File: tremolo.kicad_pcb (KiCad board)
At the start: 2 copper layers, 54 x 60 mm, 59 parts, among them J1 Jack-DC, J4 Conn_01x01_Female, J5 Conn_01x01_Female, Q1 MMBT3904, SW1 SW_Push, SW3 SW_Rotary8, SW4 SW_Rotary8, U1 TAPLFO3, U2 L78L05_SOT89, U3 VTL5C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

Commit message: cleanup
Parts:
- moved C11 32.7 mm to (92.6, 102.0), turned to 180 degrees
- moved SW1 24.1 mm to (92.5, 123.4), turned to 90 degrees
- moved R11 13.8 mm to (74.5, 102.2), turned to 0 degrees
- moved C8 12.8 mm to (113.5, 105.0)
- moved J1 12.1 mm to (72.3, 118.6), turned to 90 degrees
- moved R17 11.7 mm to (116.0, 105.0)
- moved C7 11.5 mm to (77.0, 105.2)
- moved J4 11.0 mm to (88.5, 138.5)
- moved R15 10.9 mm to (72.0, 105.2), turned to 90 degrees
- moved C6 10.7 mm to (80.6, 117.8)
- moved U2 9.86 mm to (79.8, 122.2)
- moved R31 8.94 mm to (108.0, 105.0), turned to -90 degrees
- moved C5 8.76 mm to (79.2, 127.2)
- moved R4 7.22 mm to (74.5, 111.2), turned to 90 degrees
- moved R18 6.27 mm to (113.0, 114.8)
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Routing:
- net /tap_in: track 29.9 -> 3.24 mm
- net /waveform: track 17.9 -> 34.9 mm
- net /multiplier: track 18.8 -> 29.8 mm
- net Net-(D2-Pad1): track 20.9 -> 12.7 mm
- net Net-(C11-Pad1): track 73.8 -> 67.3 mm
- net Net-(R24-Pad1): track 7.83 -> 2.47 mm
- net /sig_in: track 9.24 -> 5.57 mm
- net Net-(R30-Pad1): track 30.8 -> 27.2 mm
- net Net-(R21-Pad2): track 2.64 -> 5.71 mm
- net GND: track 4.99 -> 7.60 mm, vias 37 -> 32
- net /tempo: track 31.7 -> 29.4 mm
- net /level: track 31.3 -> 29.0 mm
- net /distort: track 31.4 -> 29.1 mm
- net Net-(R11-Pad1): track 7.83 -> 5.79 mm
- net /lfo_pwm: track 9.64 -> 11.0 mm
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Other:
- net class Default removed
- board text removed: "+"

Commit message: Cleanup
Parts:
- moved J4 29.2 mm to (117.4, 134.1), turned to 90 degrees
- moved D2 28.5 mm to (86.6, 130.8)
- moved R18 27.1 mm to (87.6, 124.2), turned to -90 degrees
- moved C9 26.4 mm to (113.9, 135.1), turned to 0 degrees
- moved J5 24.1 mm to (117.4, 118.1), turned to 90 degrees
- moved R28 24.0 mm to (113.9, 132.6), turned to 180 degrees
- moved U3 23.6 mm to (91.0, 129.0), turned to 0 degrees
- moved R26 22.8 mm to (109.9, 135.1), turned to 0 degrees
- moved R21 22.7 mm to (85.0, 124.2), turned to -90 degrees
- moved R9 20.7 mm to (114.9, 125.6), turned to 0 degrees
- moved R29 20.0 mm to (114.4, 118.1), turned to -90 degrees
- moved R30 20.0 mm to (109.9, 132.6), turned to 0 degrees
- moved C10 16.6 mm to (111.9, 118.1), turned to -90 degrees
- moved Q1 16.4 mm to (90.8, 124.2), turned to 180 degrees
- moved U4 15.9 mm to (108.9, 129.6), turned to 90 degrees
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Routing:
- net +9V: track 45.7 -> 68.0 mm
- net Net-(R30-Pad1): track 27.2 -> 6.34 mm
- net Net-(C11-Pad1): track 67.3 -> 47.7 mm
- net /tap_in: track 3.24 -> 16.0 mm
- net +5V: track 134.7 -> 126.2 mm
- net Net-(R21-Pad2): track 5.71 -> 13.4 mm
- net /lfo_pwm: track 11.0 -> 3.46 mm
- net Net-(C10-Pad2): track 50.9 -> 43.8 mm
- net GND: track 7.60 -> 3.25 mm, vias 32 -> 26
- net /multiplier: track 29.8 -> 27.5 mm
- net Net-(D2-Pad1): track 12.7 -> 10.4 mm
- net /waveform: track 34.9 -> 34.1 mm
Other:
- board size 54 x 60 mm -> 54 x 57 mm

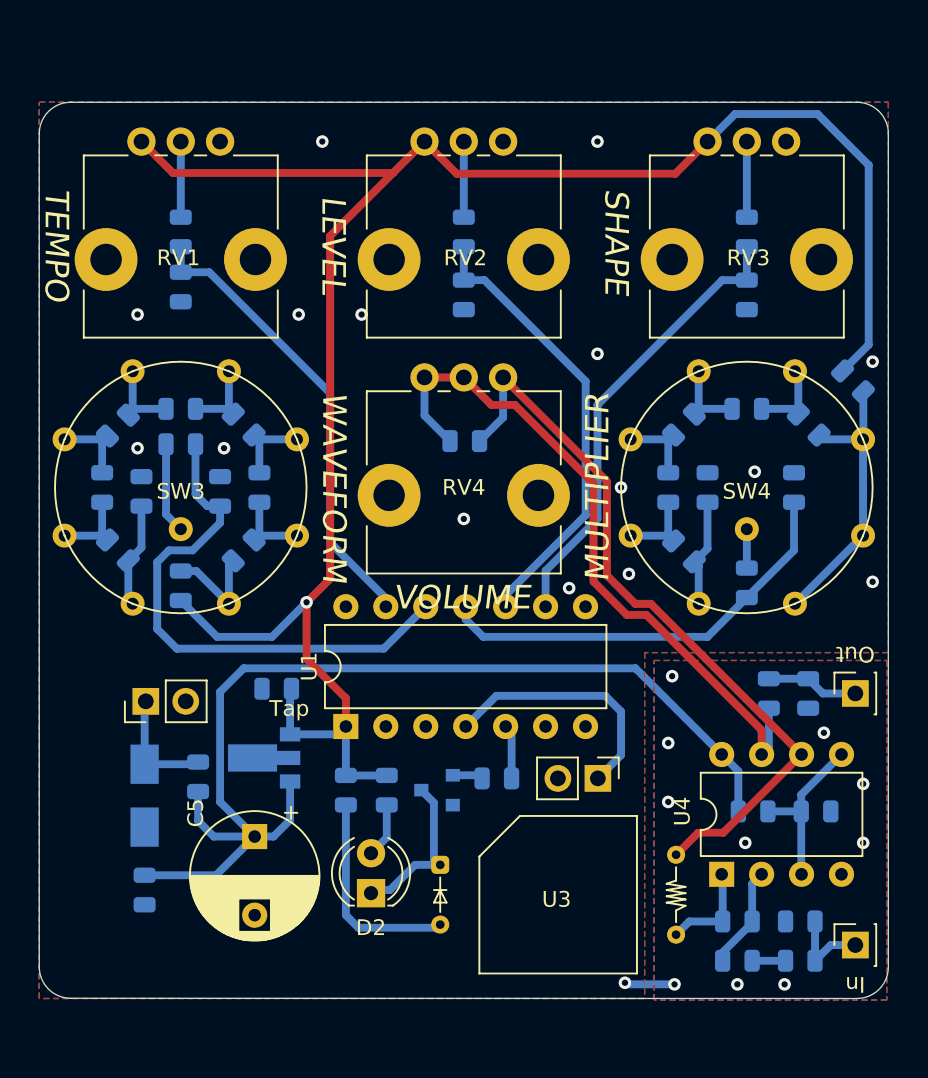
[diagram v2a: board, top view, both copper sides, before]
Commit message: Separate IO from main board
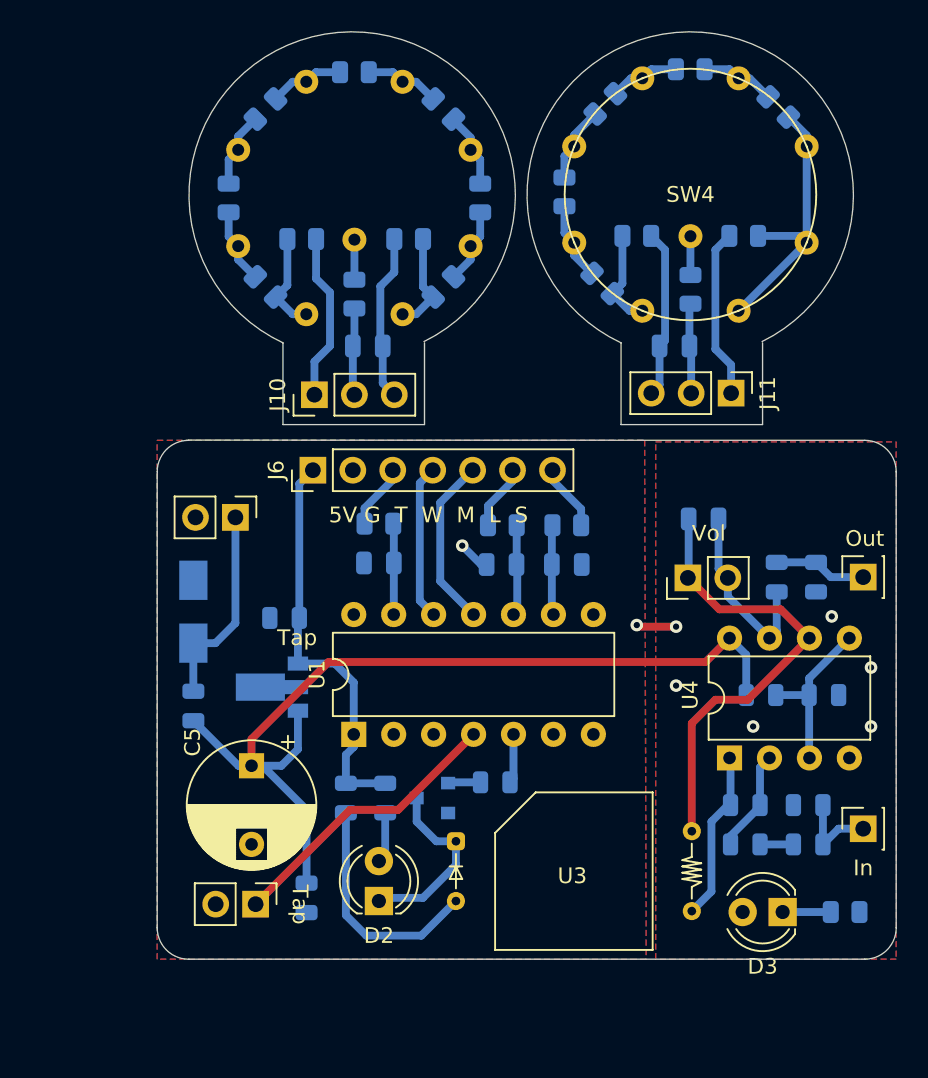
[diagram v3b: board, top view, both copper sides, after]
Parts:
- removed RV1, RV2, RV3: 10k B, Potentiometer_THT:Potentiometer_Alps_RK09L_Single_Vertical
- added D3: ACTIVE, LED_THT:LED_D4.0mm, F.Cu at (112.8, 132.0)
- added J10: Conn_01x03, Connector_PinHeader_2.54mm:PinHeader_1x03_P2.54mm_Vertical, F.Cu at (83.0, 99.1)
- added J11: Conn_01x03, Connector_PinHeader_2.54mm:PinHeader_1x03_P2.54mm_Vertical, F.Cu at (109.5, 99.0)
- added J6: Conn_01x07, Connector_PinHeader_2.54mm:PinHeader_1x07_P2.54mm_Vertical, F.Cu at (82.9, 103.9)
- added R32: 180, Resistor_SMD:R_0805_2012Metric, B.Cu at (116.8, 132.0)
- R10, R6: value 10k -> 4.7k
- R11, R24: value 1k -> 10k
- R15: value 4.7k -> 10k
- R17: value 25k -> 1k
- R20: value 10k -> 25k
- R4: value 4.7k -> 1k
- RV4: footprint Potentiometer_THT:Potentiometer_Alps_RK09L_Single_Vertical -> Connector_PinHeader_2.54mm:PinHeader_1x02_P2.54mm_Vertical
- SW3: moved to B.Cu
- moved R16 32.1 mm to (93.5, 86.6), turned to 90 degrees
- moved R24 31.8 mm to (101.5, 80.6), turned to -135 degrees
- moved R15 31.0 mm to (91.2, 80.9), turned to -45 degrees
- moved R14 30.9 mm to (85.5, 78.6), turned to 0 degrees
- moved SW1 23.2 mm to (79.3, 131.5)
- moved R23 22.6 mm to (106.9, 78.4), turned to 180 degrees
- moved R1 22.4 mm to (87.1, 107.3), turned to 0 degrees
- moved R6 22.4 mm to (89.0, 89.2), turned to 180 degrees
- moved R13 22.2 mm to (79.9, 80.9), turned to 45 degrees
- moved R3 21.9 mm to (99.0, 107.4), turned to 180 degrees
- moved C1 21.6 mm to (87.1, 109.8), turned to 180 degrees
- moved R4 21.6 mm to (85.5, 92.7), turned to -90 degrees
- moved SW3 21.5 mm to (85.5, 86.6)
- moved RV4 21.1 mm to (106.8, 110.8), turned to 90 degrees
- moved C3 20.6 mm to (99.0, 109.9), turned to 0 degrees
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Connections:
- C11 pad 1: Net-(C11-Pad1) -> Net-(U4B--)
- C7 pad 1: /waveform -> /waveform/waveform
- C7 pad 2: GND -> /waveform/GND
- C8 pad 1: /multiplier -> /multiplier/multiplier
- C8 pad 2: GND -> /multiplier/GND
- R1 pad 1: Net-(R1-Pad1) -> /tempo_RC
- R10 pad 1: Net-(R10-Pad1) -> /waveform/+5V
- R11 pad 1: Net-(R11-Pad1) -> Net-(R10-Pad2)
- R11 pad 2: /waveform -> Net-(R11-Pad2)
- R12 pad 1: Net-(R10-Pad2) -> Net-(R11-Pad2)
- R14 pad 1: Net-(R14-Pad1) -> Net-(R13-Pad2)
- R14 pad 2: Net-(R13-Pad2) -> Net-(R14-Pad2)
- R15 pad 1: Net-(R15-Pad1) -> Net-(R14-Pad2)
- R15 pad 2: GND -> Net-(R15-Pad2)
- R16 pad 1: Net-(R14-Pad1) -> Net-(R16-Pad1)
- R16 pad 2: Net-(R15-Pad1) -> Net-(R15-Pad2)
- R17 pad 1: +5V -> Net-(R17-Pad1)
- R17 pad 2: Net-(R17-Pad2) -> /multiplier/multiplier
- R2 pad 1: Net-(R2-Pad1) -> /level_RC
- R20 pad 1: Net-(R17-Pad2) -> /multiplier/+5V
- R24 pad 1: Net-(R24-Pad1) -> Net-(R23-Pad2)
- R24 pad 2: /multiplier -> Net-(R24-Pad2)
- R25 pad 1: Net-(R23-Pad2) -> Net-(R24-Pad2)
- R3 pad 1: Net-(R3-Pad1) -> /distort_RC
- R31 pad 1: GND -> /multiplier/GND
- R4 pad 1: +5V -> Net-(R4-Pad1)
- R4 pad 2: Net-(R4-Pad2) -> /waveform/waveform
- R6 pad 1: Net-(R4-Pad2) -> Net-(R6-Pad1)
- R6 pad 2: Net-(R6-Pad2) -> /waveform/GND
- R8 pad 1: Net-(R6-Pad2) -> Net-(R16-Pad1)
- R8 pad 2: Net-(R10-Pad1) -> Net-(R6-Pad1)
- RV4 pad 1: Net-(C10-Pad2) -> Net-(U4B--)
- SW3 pad 1: Net-(R4-Pad2) -> Net-(R10-Pad2)
- SW3 pad 2: Net-(R6-Pad2) -> Net-(R11-Pad2)
- SW3 pad 3: Net-(R10-Pad1) -> Net-(R12-Pad2)
- SW3 pad 4: Net-(R10-Pad2) -> Net-(R13-Pad2)
- SW3 pad 5: Net-(R12-Pad2) -> Net-(R14-Pad2)
- SW3 pad 6: Net-(R13-Pad2) -> Net-(R15-Pad2)
- SW3 pad 7: Net-(R14-Pad1) -> Net-(R16-Pad1)
- SW3 pad 8: Net-(R15-Pad1) -> Net-(R6-Pad1)
- SW3 pad 9: Net-(R11-Pad1) -> Net-(R4-Pad1)
- SW4 pad 1: Net-(R17-Pad2) -> Net-(R20-Pad2)
- SW4 pad 2: Net-(R17-Pad2) -> Net-(R20-Pad2)
- SW4 pad 3: Net-(R17-Pad2) -> Net-(R20-Pad2)
- SW4 pad 4: Net-(R20-Pad2) -> Net-(R22-Pad2)
- SW4 pad 5: Net-(R22-Pad2) -> Net-(R23-Pad2)
- SW4 pad 6: Net-(R23-Pad2) -> Net-(R24-Pad2)
- SW4 pad 9: Net-(R24-Pad1) -> Net-(R17-Pad1)
- U1 pad 2: (no net) -> unconnected-(U1-CV_INVERT-Pad2)
- U1 pad 7: (no net) -> unconnected-(U1-CLOCK_OUT-Pad7)
- U1 pad 8: (no net) -> unconnected-(U1-BIPOLAR-Pad8)
- U3 pad 4: Net-(C11-Pad1) -> Net-(U4B--)
- U4 pad 6: Net-(C11-Pad1) -> Net-(U4B--)
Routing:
- net +5V: track 126.2 -> 25.9 mm, vias 1 -> 0
- net Net-(C11-Pad1): track 47.7 -> 0.00 mm
- net Net-(C10-Pad2): track 43.8 -> 12.1 mm
- net Net-(U4B--): track 0.00 -> 29.7 mm
- net /waveform: track 34.1 -> 9.91 mm
- net /tempo: track 29.4 -> 5.82 mm
- net /distort: track 29.1 -> 5.74 mm
- net /level: track 29.0 -> 5.81 mm
- net Net-(R17-Pad2): track 18.2 -> 0.00 mm
- net /multiplier: track 27.5 -> 10.9 mm
- net Net-(R20-Pad2): track 5.29 -> 17.9 mm
- net /multiplier/+5V: track 0.00 -> 10.8 mm
- net /multiplier/GND: track 0.00 -> 10.7 mm
- net /waveform/+5V: track 0.00 -> 10.7 mm
- net /waveform/GND: track 0.00 -> 10.6 mm
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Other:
- board size 54 x 57 mm -> 47 x 59 mm
- board text added: "5V G T W M L S"
- board text added: "Vol"
- board text removed: "LEVEL"
- board text removed: "MULTIPLIER"
- board text removed: "SHAPE"
- board text removed: "TEMPO"
- board text removed: "VOLUME"
- board text removed: "WAVEFORM"

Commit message: THT version
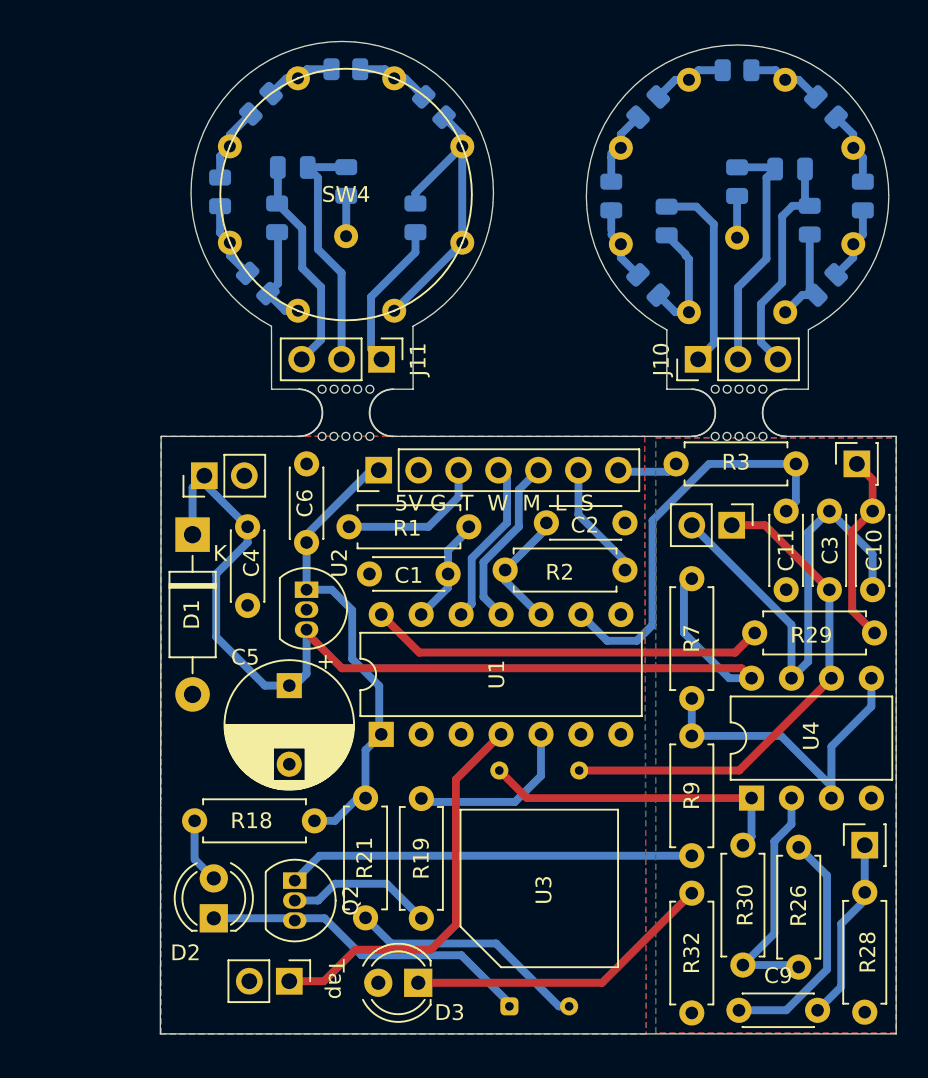
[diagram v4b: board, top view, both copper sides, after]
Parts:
- removed Q1: MMBT3904, Package_TO_SOT_SMD:SOT-23
- removed R5: 0, Resistor_SMD:R_0805_2012Metric
- added Q2: 2N3904, Package_TO_SOT_THT:TO-92_Inline, F.Cu at (81.8, 130.0)
- added mouse-bite-3mm-slot: VAL**, Panelization:mouse-bite-3mm-slot, F.Cu at (85.0, 100.2)
- added mouse-bite-3mm-slot: VAL**, Panelization:mouse-bite-3mm-slot, F.Cu at (110.0, 100.2)
- C1, C10, C11, C2, C3, C4, C6, C9: footprint Capacitor_SMD:C_0805_2012Metric -> Capacitor_THT:C_Disc_D4.3mm_W1.9mm_P5.00mm; moved to F.Cu
- D1: value US1B -> 1N4001; footprint Diode_SMD:D_SMA -> Diode_THT:D_DO-41_SOD81_P10.16mm_Horizontal; moved to F.Cu
- R1, R18, R19, R2, R21, R26, R28, R29, R3, R30, R32, R7, R9: footprint Resistor_SMD:R_0805_2012Metric -> Resistor_THT:R_Axial_DIN0207_L6.3mm_D2.5mm_P7.62mm_Horizontal; moved to F.Cu
- U2: footprint Package_TO_SOT_SMD:SOT-89-3 -> Package_TO_SOT_THT:TO-92L_Inline; moved to F.Cu
- moved C7 29.1 mm to (113.2, 84.8)
- moved C8 26.8 mm to (81.6, 84.7)
- moved R6 25.5 mm to (114.5, 88.0), turned to 90 degrees
- moved R4 25.4 mm to (109.9, 85.6), turned to 90 degrees
- moved J10 24.5 mm to (107.4, 96.8)
- moved R11 24.3 mm to (104.2, 92.1)
- moved R12 24.3 mm to (101.9, 86.5)
- moved R13 24.3 mm to (104.2, 80.8)
- moved R14 24.3 mm to (109.9, 78.5)
- moved R15 24.3 mm to (115.5, 80.8)
- moved R16 24.3 mm to (117.9, 86.5)
- moved R8 24.3 mm to (115.5, 92.1)
- moved SW3 24.3 mm to (109.9, 86.5)
- moved C4 23.9 mm to (78.8, 107.5)
- moved D3 23.6 mm to (89.6, 136.5)
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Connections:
- D1 pad 1: /VIN -> +9V
- J1 pad 1: /VIN -> +9V
- R32 pad 2: /IO/GND -> GND
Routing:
- net GND: track 4.59 -> 51.2 mm, vias 8 -> 0
- net /distort: track 5.74 -> 26.2 mm
- net Net-(C10-Pad2): track 12.1 -> 30.1 mm
- net Net-(D3-K): track 3.06 -> 19.8 mm
- net Net-(C9-Pad1): track 2.12 -> 15.2 mm
- net /VIN: track 13.0 -> 0.00 mm
- net /+4V5: track 10.8 -> 22.0 mm
- net /waveform/waveform: track 5.57 -> 15.5 mm
- net /multiplier/multiplier: track 5.76 -> 15.6 mm
- net Net-(D2-K): track 11.9 -> 21.4 mm
- net Net-(R30-Pad1): track 10.9 -> 20.0 mm
- net Net-(U4A--): track 6.53 -> 15.5 mm
- net /lfo_pwm: track 3.14 -> 11.0 mm
- net Net-(Q2-B): track 2.08 -> 9.40 mm
- net /tap_in: track 18.3 -> 25.4 mm
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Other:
- board size 47 x 59 mm -> 46.8 x 63.1 mm
- board text removed: "In"
- board text removed: "Out"
- board text removed: "Vol"
